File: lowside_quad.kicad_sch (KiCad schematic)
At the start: 4 parts

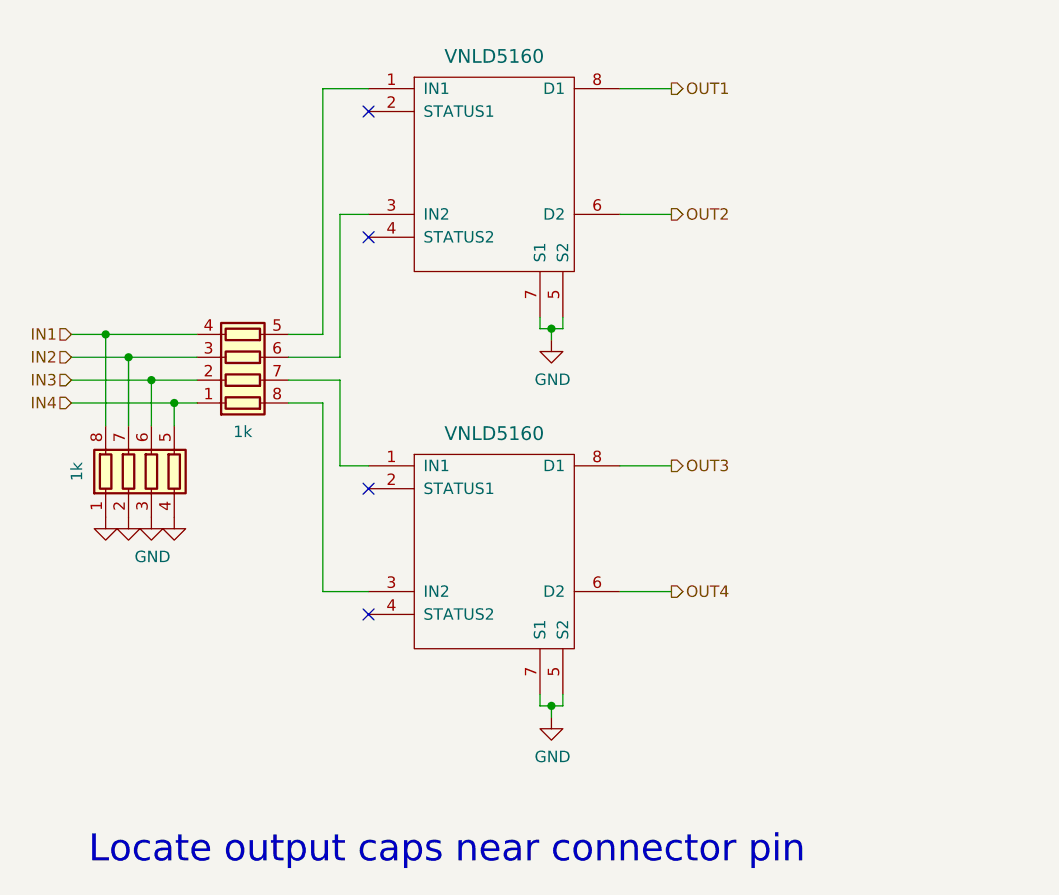
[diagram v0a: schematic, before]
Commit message: пронумеровала, перенесла изменения на плату
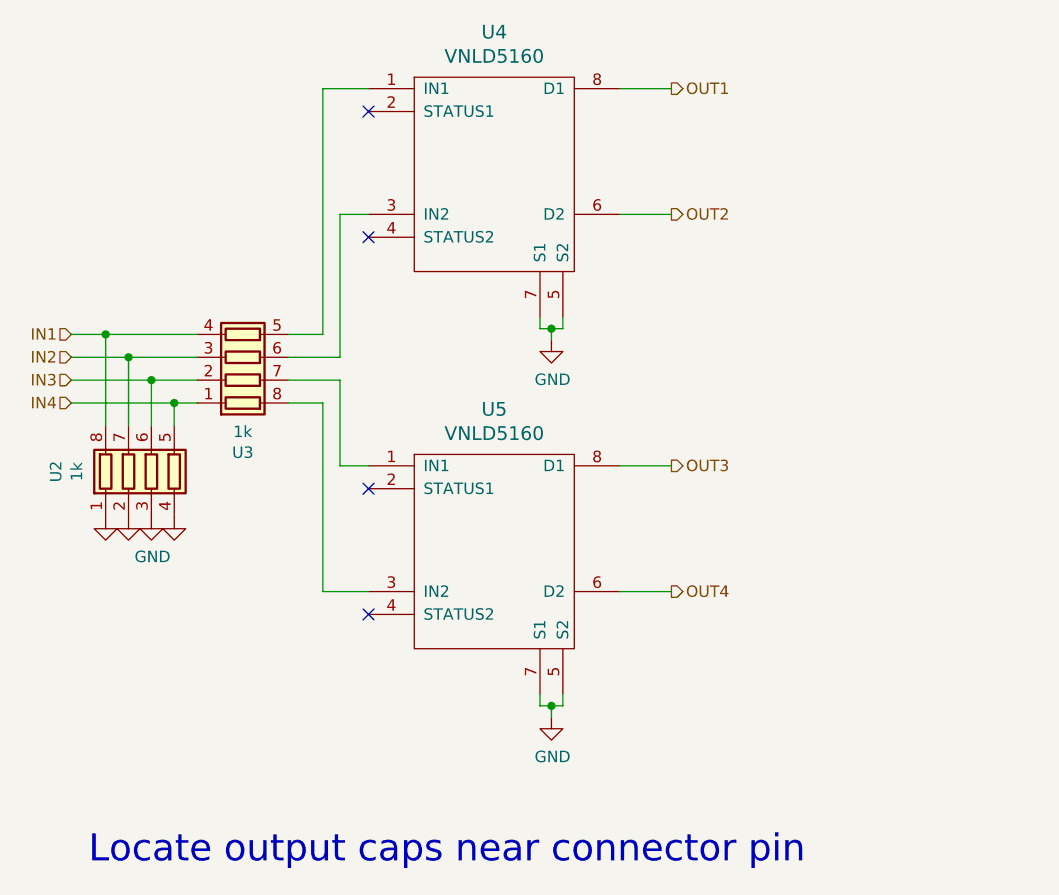
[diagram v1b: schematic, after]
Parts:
- gave numbers to parts that had none: 4

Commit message: Upd SCH
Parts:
- renumbered U2 to R44, U3 to R45
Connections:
- net IN1: now also R45.5 (R4.2); no longer R45.4 (R4.1)
- net IN2: now also R45.6 (R3.2); no longer R45.3 (R3.1)
- net IN3: now also R45.7 (R2.2); no longer R45.2 (R2.1)
- net IN4: now also R45.8 (R1.2); no longer R45.1 (R1.1)
- net at U4.1 (IN1): now also R45.4 (R4.1); no longer R45.5 (R4.2)
- net at U4.3 (IN2): now also R45.3 (R3.1); no longer R45.6 (R3.2)
- net at U5.1 (IN1): now also R45.2 (R2.1); no longer R45.7 (R2.2)
- net at U5.3 (IN2): now also R45.1 (R1.1); no longer R45.8 (R1.2)
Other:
- moved on the sheet: R44, R45, U4, U5

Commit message: Export
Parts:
- U4, U5: LCSC N/A -> C377942
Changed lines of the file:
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@@
       (effects (font (size 1.27 1.27)) hide)
     )
-    (property "LCSC" "N/A" (at 106.68 52.07 0)
+    (property "LCSC" "C377942" (at 106.68 52.07 0)
       (effects (font (size 1.27 1.27)) hide)
     )
@@
       (effects (font (size 1.27 1.27)) hide)
     )
-    (property "LCSC" "N/A" (at 106.68 93.98 0)
+    (property "LCSC" "C377942" (at 106.68 93.98 0)
       (effects (font (size 1.27 1.27)) hide)
     )

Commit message: MM100_0.2
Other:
- note removed: "Locate output caps near connector pin"
- title: rusEfi Proteus -> (none)
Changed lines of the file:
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@@
   (paper "A4")
   (title_block
-    (title "rusEfi Proteus")
-    (date "2022-04-09")
-    (rev "v0.7")
+    (date "2023-10-01")
     (company "rusEFI")
-    (comment 1 "github.com/mck1117/proteus")
-    (comment 2 "rusefi.com/s/proteus")
   )
   (junction (at 68.58 73.66) (diameter 0) (color 0 0 0 0)
@@
     (stroke (width 0) (type default))
   )
-  (text "Locate output caps near connector pin" (at 60.96 127.635 0)
-    (effects (font (size 2.9972 2.9972)) (justify left bottom))
-  )
   (hierarchical_label "OUT3" (shape output) (at 125.73 83.82 0) (fields_autoplaced)
